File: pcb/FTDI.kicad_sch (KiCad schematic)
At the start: 49 parts, among them J3 USB3_B_micro, U3 FT600Q-B-x, Y1 30MHz

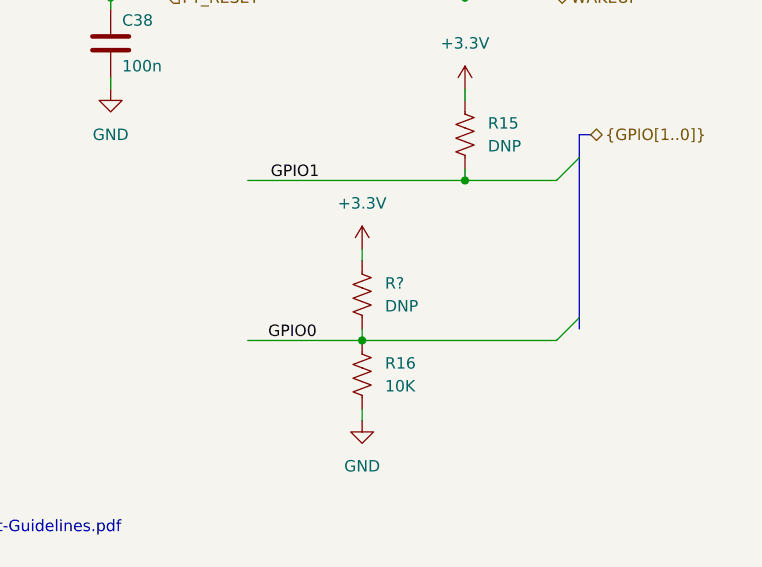
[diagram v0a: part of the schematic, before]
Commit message: Fix some ERC errors
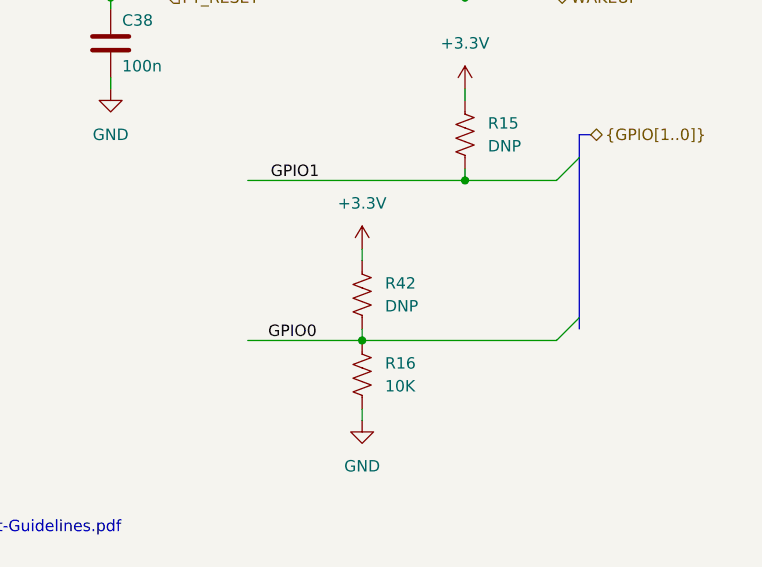
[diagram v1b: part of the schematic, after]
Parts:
- gave numbers to parts that had none: 1
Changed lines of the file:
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@@
   (symbol (lib_id "power:+3.3V") (at 237.49 133.35 0) (unit 1)
     (in_bom yes) (on_board yes) (fields_autoplaced)
-    (property "Reference" "#PWR?" (id 0) (at 237.49 137.16 0)
+    (property "Reference" "#PWR039" (id 0) (at 237.49 137.16 0)
       (effects (font (size 1.27 1.27)) hide)
     )
@@
   (symbol (lib_id "Device:R_US") (at 237.49 138.43 0) (unit 1)
     (in_bom yes) (on_board yes) (fields_autoplaced)
-    (property "Reference" "R?" (id 0) (at 240.03 137.1599 0)
-      (effects (font (size 1.27 1.27)) (justify left))
-    )
+    (property "Reference" "R42" (id 0) (at 240.03 137.1599 0)
+      (effects (font (size 1.27 1.27)) (justify left))
+    )

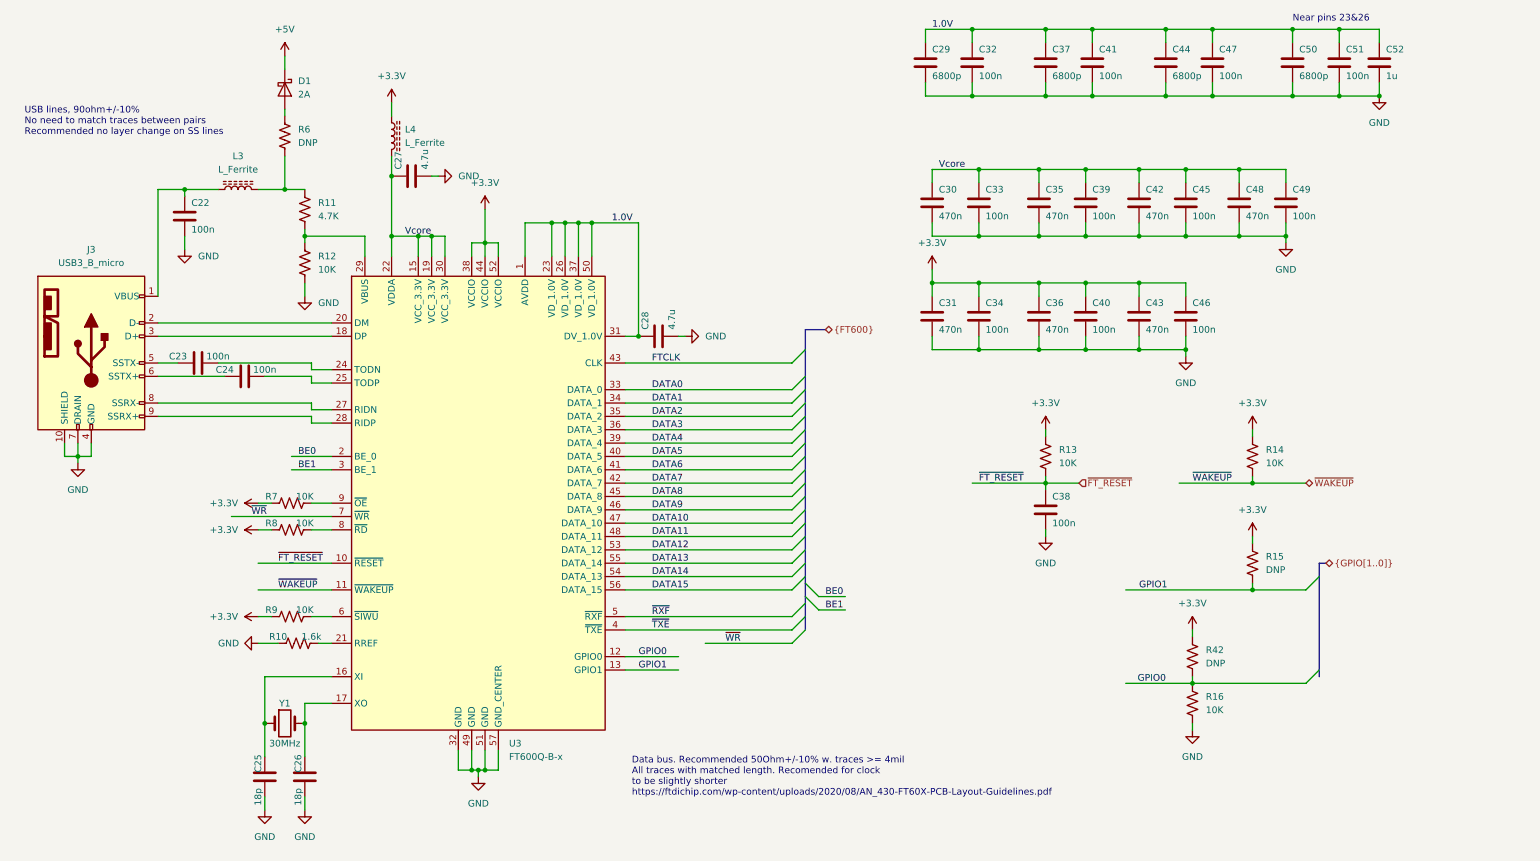
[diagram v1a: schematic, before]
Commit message: Add filter and ESD protection to USB inputs
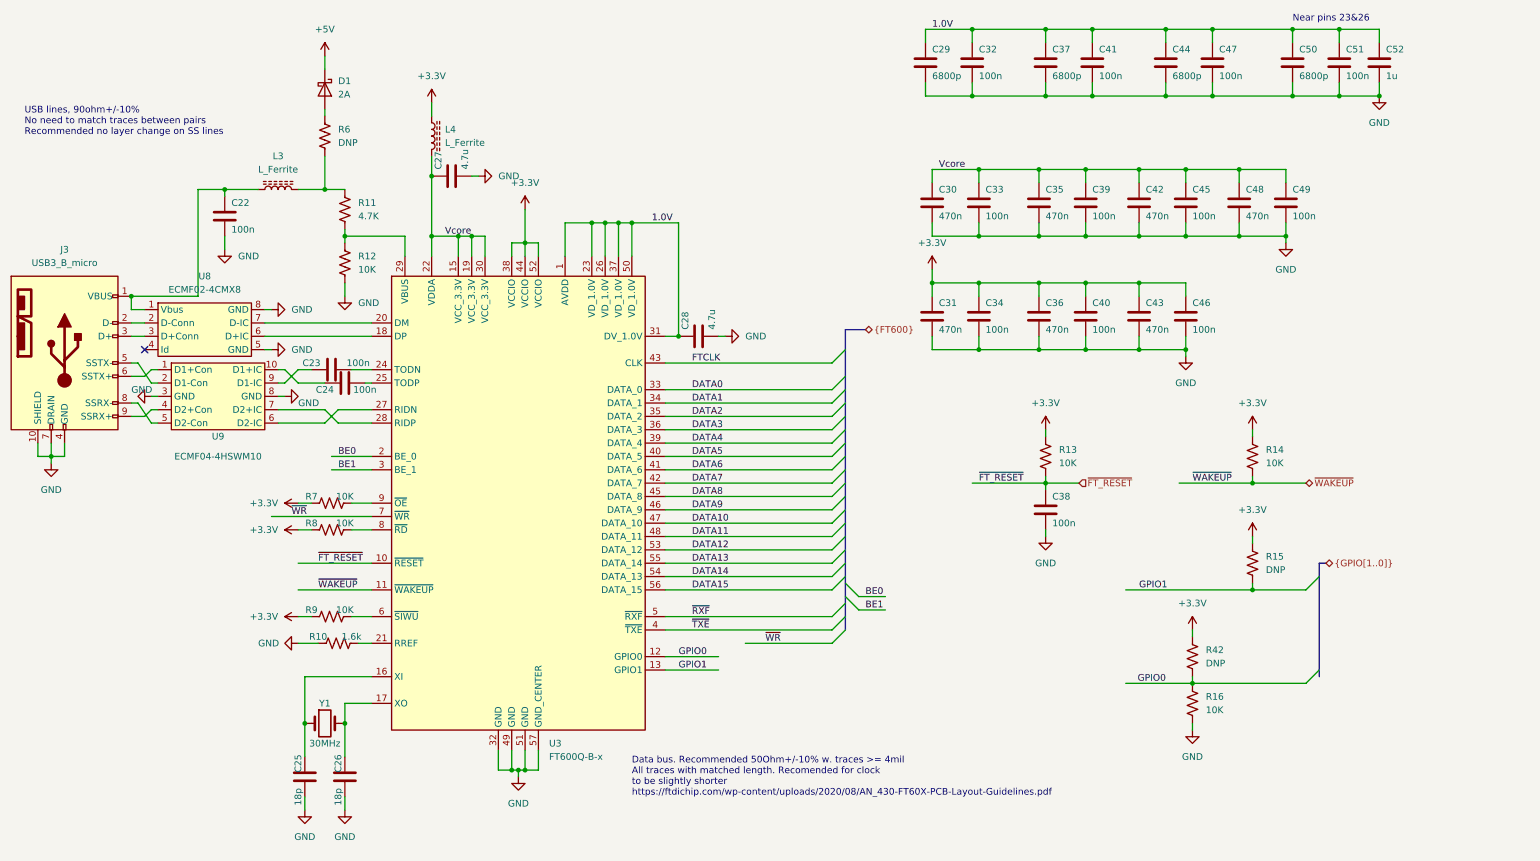
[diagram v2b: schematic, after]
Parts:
- added U8: ECMF02-4CMX8, symbol ecp5u85-bse-usb:ECMF02-4CMX8
- added U9: ECMF04-4HSWM10, symbol ecp5u85-bse-usb:ECMF04-4HSWM10
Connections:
- net GND: now also U8.5 (GND), U8.8 (GND), U9.3 (GND), U9.8 (GND)
- net at C22.1, J3.1 (VBUS), L3.1: now also U8.1 (Vbus)
- net at J3.3 (D+): now also U8.3 (D+Conn); no longer U3.18 (DP)
- net at J3.2 (D-): now also U8.2 (D-Conn); no longer U3.20 (DM)
- net at U3.27 (RIDN): now also U9.6 (D2-IC); no longer J3.8 (SSRX-)
- net at U3.28 (RIDP): now also U9.7 (D2+IC); no longer J3.9 (SSRX+)
- net at J3.5 (SSTX-): now also U9.2 (D1-Con); no longer C23.1
- net at J3.6 (SSTX+): now also U9.1 (D1+Con); no longer C24.1
- new net: U3.18 (DP), U8.6 (D+IC)
- new net: U3.20 (DM), U8.7 (D-IC)
- new net: C24.1, U9.10 (D1+IC)
- new net: J3.9 (SSRX+), U9.4 (D2+Con)
- new net: J3.8 (SSRX-), U9.5 (D2-Con)
- new net: C23.1, U9.9 (D1-IC)
- no-connect marks 0 -> 1
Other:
- moved on the sheet: C22, C23, C24, C25, C26, C27, C28, D1, J3, L3, L4, R10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

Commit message: Fix some symbols
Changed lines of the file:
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@@
+    (pin "1")
+  )
+  (symbol (lib_id "power:PWR_FLAG") (at 92.71 46.99 90) (unit 1)
+    (in_bom yes) (on_board yes) (fields_autoplaced)
+    (property "Reference" "#FLG0103" (id 0) (at 90.805 46.99 0)
+      (effects (font (size 1.27 1.27)) hide)
+    )
+    (property "Value" "PWR_FLAG" (id 1) (at 88.9 46.9899 90)
+      (effects (font (size 1.27 1.27)) (justify left))
+    )
+    (property "Footprint" "" (id 2) (at 92.71 46.99 0)
+      (effects (font (size 1.27 1.27)) hide)
+    )
+    (property "Datasheet" "~" (id 3) (at 92.71 46.99 0)
+      (effects (font (size 1.27 1.27)) hide)
+    )
     (pin "1")
   )

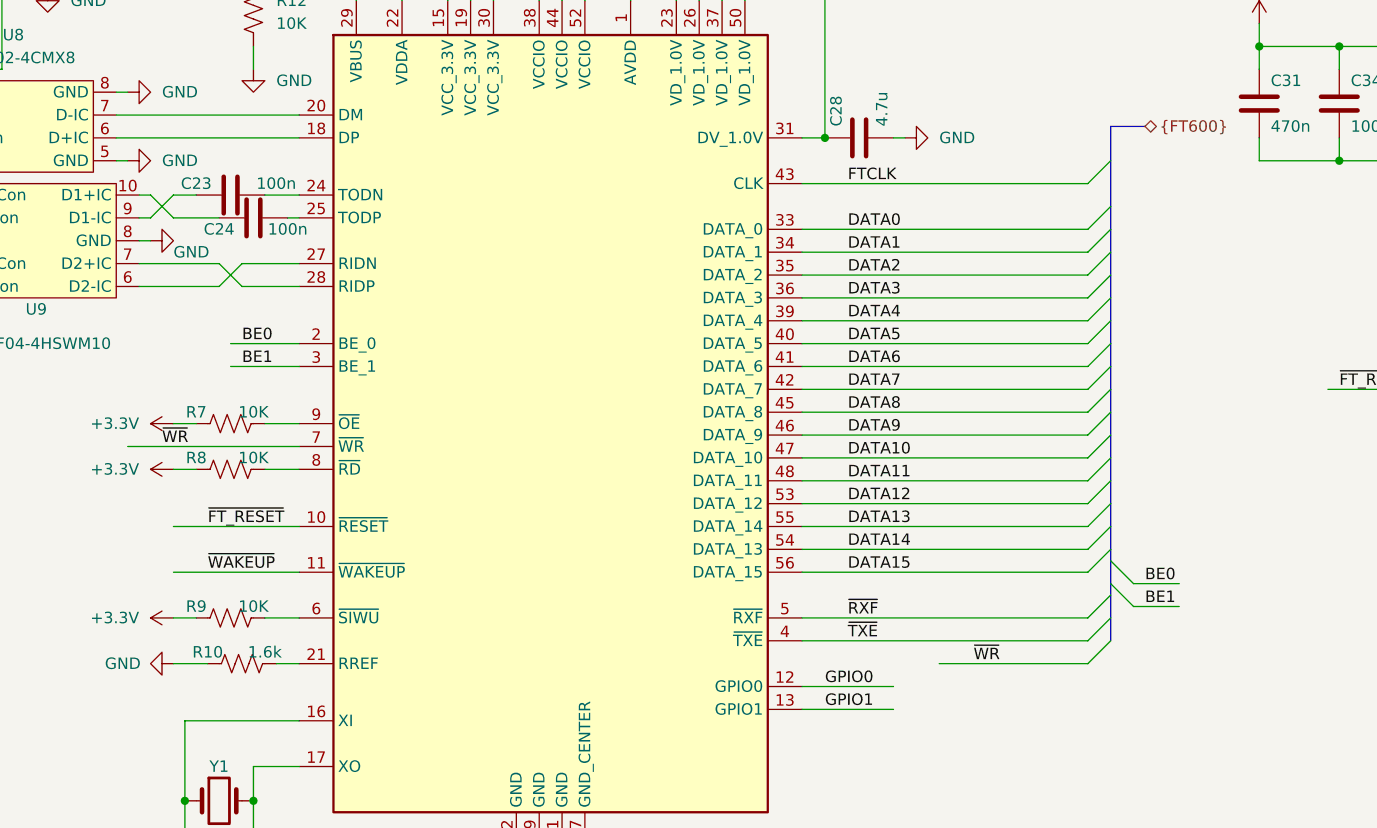
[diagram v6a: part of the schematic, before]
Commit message: Rename FTDI nets to include prefix
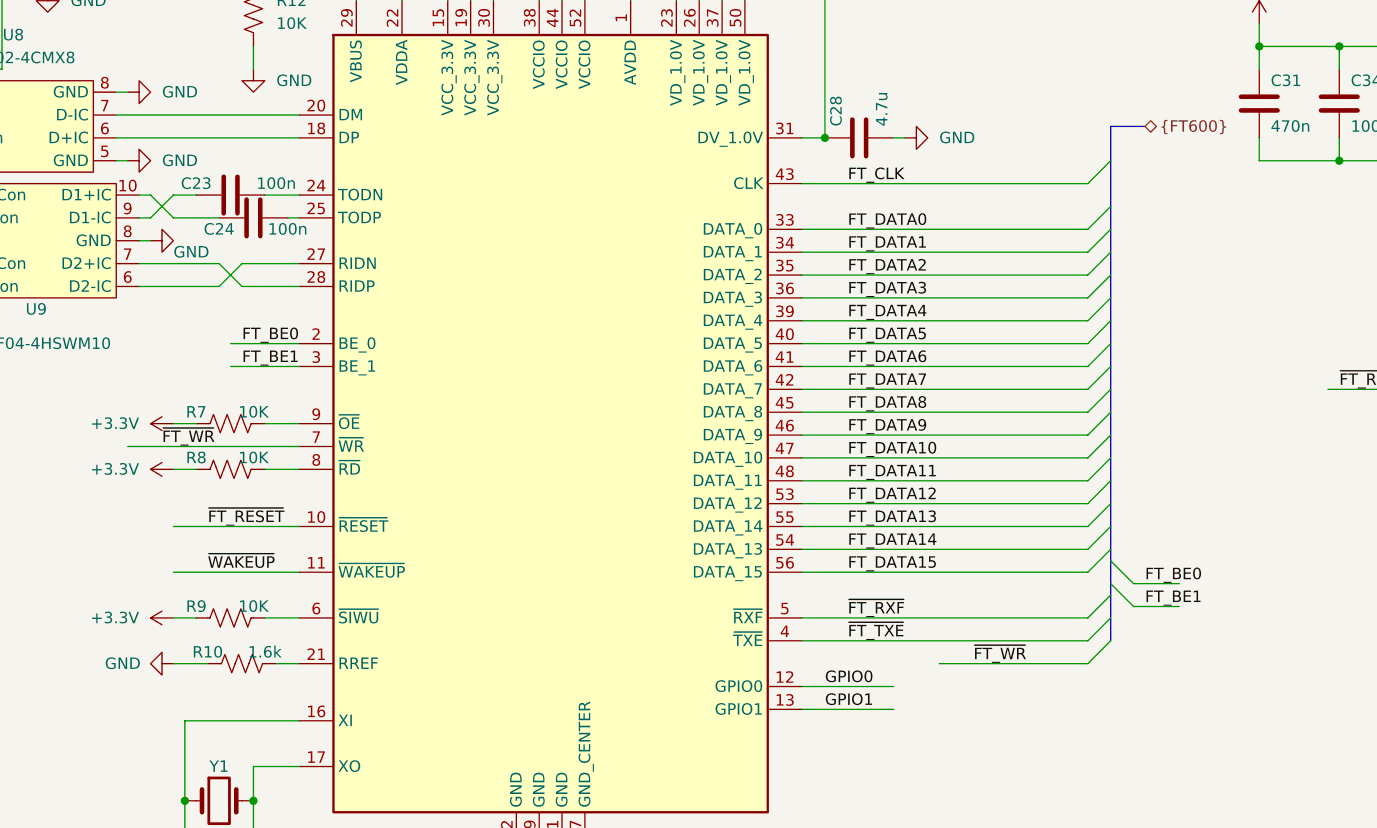
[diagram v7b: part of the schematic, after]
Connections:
- net BE0 renamed FT_BE0
- net BE1 renamed FT_BE1
- net DATA0 renamed FT_DATA0
- net DATA1 renamed FT_DATA1
- net DATA10 renamed FT_DATA10
- net DATA11 renamed FT_DATA11
- net DATA12 renamed FT_DATA12
- net DATA13 renamed FT_DATA13
- net DATA14 renamed FT_DATA14
- net DATA15 renamed FT_DATA15
- net DATA2 renamed FT_DATA2
- net DATA3 renamed FT_DATA3
- net DATA4 renamed FT_DATA4
- net DATA5 renamed FT_DATA5
- net DATA6 renamed FT_DATA6
- net DATA7 renamed FT_DATA7
- net DATA8 renamed FT_DATA8
- net DATA9 renamed FT_DATA9
- net FTCLK renamed FT_CLK
- net ~{RXF} renamed ~{FT_RXF}
- net ~{TXE} renamed ~{FT_TXE}
- net ~{WR} renamed ~{FT_WR}
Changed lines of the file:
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@@
     (comment 1 "Aarón Cuevas López")
   )
-  (bus_alias "FT600" (members "DATA[0..15]" "BE[0..1]" "~{RXF}" "~{TXE}" "~{WR}" "FTCLK"))
+  (bus_alias "FT600" (members "FT_DATA[0..15]" "FT_BE[0..1]" "~{FT_RXF}" "~{FT_TXE}" "~{FT_WR}" "FT_CLK"))
   (junction (at 97.79 58.42) (diameter 0) (color 0 0 0 0)
   )
@@
     (effects (font (size 1.27 1.27)) (justify left bottom))
   )
-  (label "DATA9" (at 142.24 110.49 0)
-    (effects (font (size 1.27 1.27)) (justify left bottom))
-  )
-  (label "DATA8" (at 142.24 107.95 0)
+  (label "FT_DATA9" (at 142.24 110.49 0)
+    (effects (font (size 1.27 1.27)) (justify left bottom))
+  )
+  (label "FT_DATA8" (at 142.24 107.95 0)
     (effects (font (size 1.27 1.27)) (justify left bottom))
   )
@@
     (effects (font (size 1.27 1.27)) (justify left bottom))
   )
-  (label "DATA0" (at 142.24 87.63 0)
-    (effects (font (size 1.27 1.27)) (justify left bottom))
-  )
-  (label "DATA11" (at 142.24 115.57 0)
-    (effects (font (size 1.27 1.27)) (justify left bottom))
-  )
-  (label "BE0" (at 175.26 127 0)
-    (effects (font (size 1.27 1.27)) (justify left bottom))
-  )
-  (label "DATA15" (at 142.24 125.73 0)
-    (effects (font (size 1.27 1.27)) (justify left bottom))
-  )
-  (label "DATA12" (at 142.24 118.11 0)
-    (effects (font (size 1.27 1.27)) (justify left bottom))
-  )
-  (label "BE0" (at 74.93 100.33 0)
+  (label "FT_DATA0" (at 142.24 87.63 0)
+    (effects (font (size 1.27 1.27)) (justify left bottom))
+  )
+  (label "FT_DATA11" (at 142.24 115.57 0)
+    (effects (font (size 1.27 1.27)) (justify left bottom))
+  )
+  (label "FT_BE0" (at 175.26 127 0)
+    (effects (font (size 1.27 1.27)) (justify left bottom))
+  )
+  (label "FT_DATA15" (at 142.24 125.73 0)
+    (effects (font (size 1.27 1.27)) (justify left bottom))
+  )
+  (label "FT_DATA12" (at 142.24 118.11 0)
+    (effects (font (size 1.27 1.27)) (justify left bottom))
+  )
+  (label "FT_BE0" (at 74.93 100.33 0)
     (effects (font (size 1.27 1.27)) (justify left bottom))
   )
@@
     (effects (font (size 1.27 1.27)) (justify left bottom))
   )
-  (label "~{RXF}" (at 142.24 130.81 0)
+  (label "~{FT_RXF}" (at 142.24 130.81 0)
     (effects (font (size 1.27 1.27)) (justify left bottom))
   )
@@
     (effects (font (size 1.27 1.27)) (justify left bottom))
   )
-  (label "~{WR}" (at 66.04 111.76 0)
-    (effects (font (size 1.27 1.27)) (justify left bottom))
-  )
-  (label "BE1" (at 74.93 102.87 0)
-    (effects (font (size 1.27 1.27)) (justify left bottom))
-  )
-  (label "BE1" (at 175.26 129.54 0)
+  (label "~{FT_WR}" (at 66.04 111.76 0)
+    (effects (font (size 1.27 1.27)) (justify left bottom))
+  )
+  (label "FT_BE1" (at 74.93 102.87 0)
+    (effects (font (size 1.27 1.27)) (justify left bottom))
+  )
+  (label "FT_BE1" (at 175.26 129.54 0)
     (effects (font (size 1.27 1.27)) (justify left bottom))
   )
@@
     (effects (font (size 1.27 1.27)) (justify left bottom))
   )
-  (label "DATA2" (at 142.24 92.71 0)
+  (label "FT_DATA2" (at 142.24 92.71 0)
     (effects (font (size 1.27 1.27)) (justify left bottom))
   )
@@
     (effects (font (size 1.27 1.27)) (justify left bottom))
   )
-  (label "~{TXE}" (at 142.24 133.35 0)
-    (effects (font (size 1.27 1.27)) (justify left bottom))
-  )
-  (label "DATA4" (at 142.24 97.79 0)
-    (effects (font (size 1.27 1.27)) (justify left bottom))
-  )
-  (label "~{WR}" (at 156.21 135.89 0)
+  (label "~{FT_TXE}" (at 142.24 133.35 0)
+    (effects (font (size 1.27 1.27)) (justify left bottom))
+  )
+  (label "FT_DATA4" (at 142.24 97.79 0)
+    (effects (font (size 1.27 1.27)) (justify left bottom))
+  )
+  (label "~{FT_WR}" (at 156.21 135.89 0)
     (effects (font (size 1.27 1.27)) (justify left bottom))
   )
@@
     (effects (font (size 1.27 1.27)) (justify left bottom))
   )
-  (label "DATA13" (at 142.24 120.65 0)
-    (effects (font (size 1.27 1.27)) (justify left bottom))
-  )
-  (label "DATA14" (at 142.24 123.19 0)
+  (label "FT_DATA13" (at 142.24 120.65 0)
+    (effects (font (size 1.27 1.27)) (justify left bottom))
+  )
+  (label "FT_DATA14" (at 142.24 123.19 0)
     (effects (font (size 1.27 1.27)) (justify left bottom))
   )
@@
     (effects (font (size 1.27 1.27)) (justify left bottom))
   )
-  (label "DATA10" (at 142.24 113.03 0)
+  (label "FT_DATA10" (at 142.24 113.03 0)
     (effects (font (size 1.27 1.27)) (justify left bottom))
   )
@@
     (effects (font (size 1.27 1.27)) (justify left bottom))
   )
-  (label "DATA7" (at 142.24 105.41 0)
-    (effects (font (size 1.27 1.27)) (justify left bottom))
-  )
-  (label "DATA3" (at 142.24 95.25 0)
+  (label "FT_DATA7" (at 142.24 105.41 0)
+    (effects (font (size 1.27 1.27)) (justify left bottom))
+  )
+  (label "FT_DATA3" (at 142.24 95.25 0)
     (effects (font (size 1.27 1.27)) (justify left bottom))
   )
@@
     (effects (font (size 1.27 1.27)) (justify left bottom))
   )
-  (label "FTCLK" (at 142.24 82.55 0)
-    (effects (font (size 1.27 1.27)) (justify left bottom))
-  )
-  (label "DATA1" (at 142.24 90.17 0)
-    (effects (font (size 1.27 1.27)) (justify left bottom))
-  )
-  (label "DATA6" (at 142.24 102.87 0)
-    (effects (font (size 1.27 1.27)) (justify left bottom))
-  )
-  (label "DATA5" (at 142.24 100.33 0)
-    (effects (font (size 1.27 1.27)) (justify left bottom))
-  )
+  (label "FT_CLK" (at 142.24 82.55 0)
+    (effects (font (size 1.27 1.27)) (justify left bottom))
+  )
+  (label "FT_DATA1" (at 142.24 90.17 0)
+    (effects (font (size 1.27 1.27)) (justify left bottom))
+  )
+  (label "FT_DATA6" (at 142.24 102.87 0)
+    (effects (font (size 1.27 1.27)) (justify left bottom))
+  )
+  (label "FT_DATA5" (at 142.24 100.33 0)
+    (effects (font (size 1.27 1.27)) (justify left bottom))
+  )
